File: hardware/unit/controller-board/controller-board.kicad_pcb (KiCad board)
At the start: 4 copper layers, 152 x 122.5 mm, 92 parts, among them J1 RJ45 LINK, J2 to RF board J14, Q4 BSS138BK, U1 VO2611, U11 LP2985-33, U12 TPS3823A-33, U13 74LVC1G74, U14 74LVC1G27, U15 74LVC1G02, U16 74LVC1G08, U2 VO2611, U3 VO2611, U4 PC817X, U5 74LVC1G14, U6 TLP176AM

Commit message: Pre-order review; RF board seat keep-outs; part reuse P-1 to P-5
- docs/reviews/2026-10-31-pre-order-review.md: review of all three boards
  before ordering (verify scripts, ERC/DRC, pin maps, BOM, fab and case,
  firmware against spec, open items, part reuse).
- RF board (D-189, M-107): no other-net copper or vias under the case
  seats at S1 to S6 and the SO-239/SMA GND bosses; relay NC pads (pad 12)
  in netclass RF. Re-routed, DRC 0.
- Part reuse (D-190, M-108): one value text for 2k2, 100n 50V X7R and
  10n 50V X7R; shack PC817X order code as the controller; shack U4/U9 in
  VSSOP-8 (TI DCU, Nexperia DC) with fixed fan-out, re-routed.
  Netlists rf15, ctl15, si17; ERC 0.

Co-Authored-By: Claude Opus 5.5 <noreply@anthropic.com>
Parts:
- C12: value 10n -> 10n 50V X7R

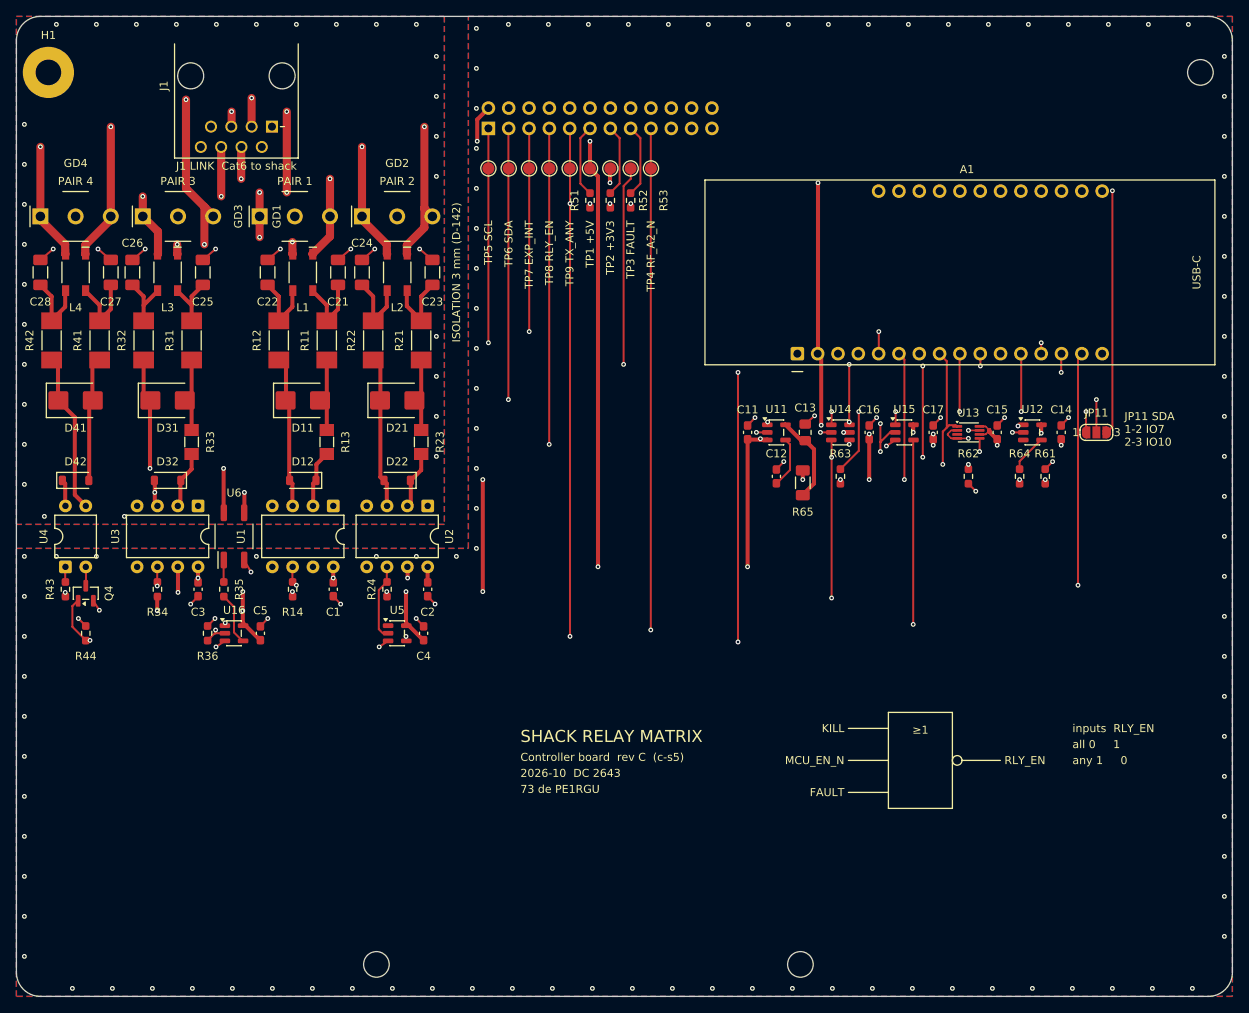
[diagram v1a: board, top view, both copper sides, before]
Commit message: S-1: FAULT to GPIO6, box fault 11, host clearfault
Hardware (D-191, M-109):
- Controller board: R66 1k from FAULT (U13 Q) to DevKit pin 11 (GPIO6).
  Schematic c15-fault-io6, netlist ctl16, layout c-s6, re-routed.
  ERC 0, DRC 0 violations and 0 unconnected. BOM: R66 on the 1k line.
- gen_controller_pcb.py splits a track where a same-net track ends on it.
- verify_logic.py checks R66 and FAULT_IO6.

Firmware:
- Box reads FAULT. After the self-test, FAULT = 1 gives fault 11
  (supervisor trip); READY stays open.
- New link command ClearFault (0x03): one LATCH_CLR edge, Ok if FAULT
  clears, else NotReady. No edge without a trip.
- Host clearfault also sends ClearFault when the box reports fault 11.
- Sim model, box target (GPIO6), 3 new tests.

Co-Authored-By: Claude Opus 5.5 <noreply@anthropic.com>
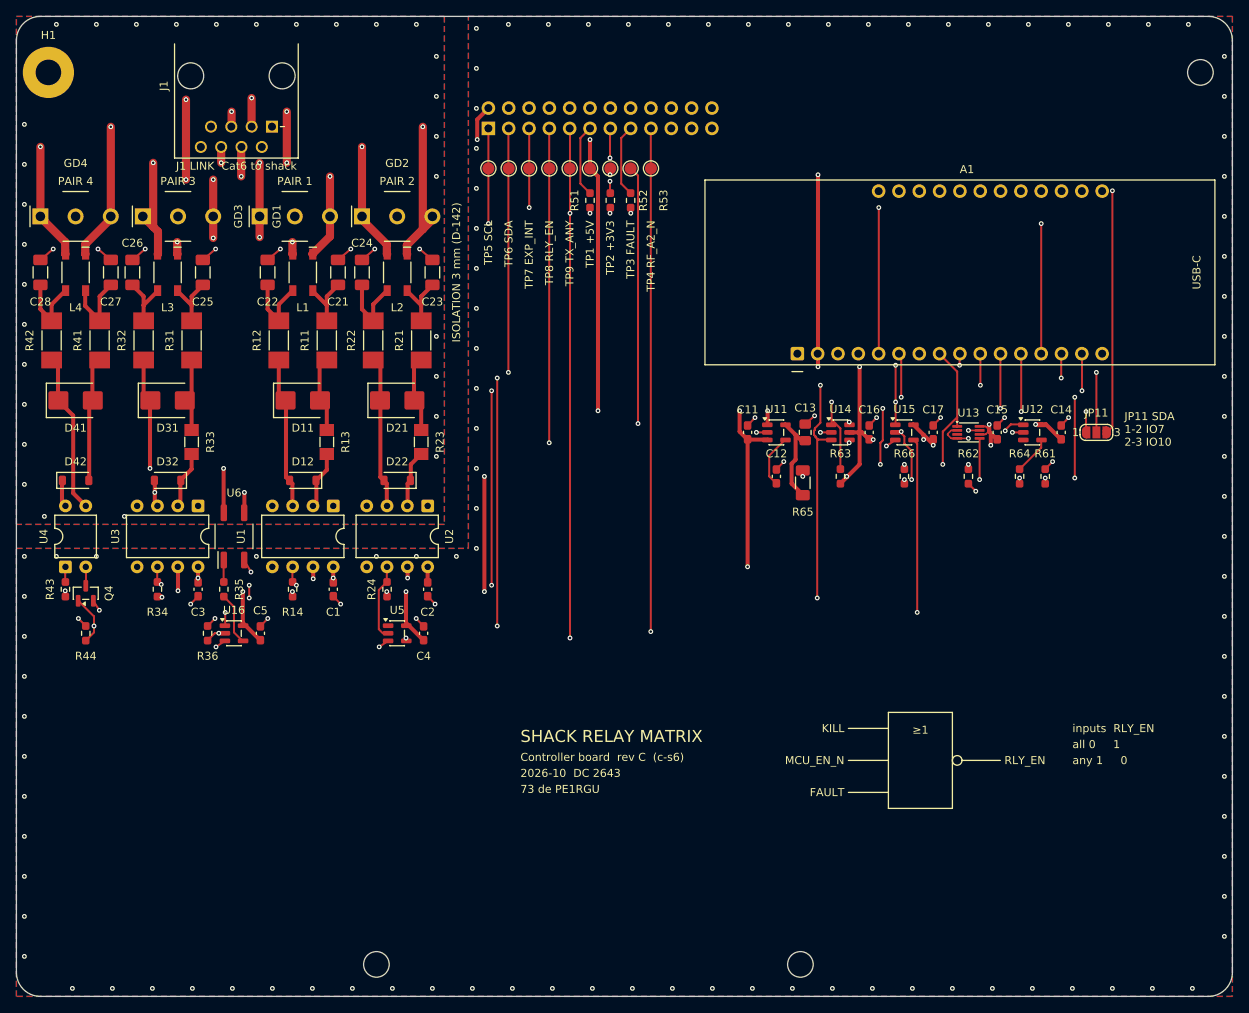
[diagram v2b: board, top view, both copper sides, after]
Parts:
- added R66: 1k, Resistor_SMD:R_0603_1608Metric_Pad0.98x0.95mm_HandSolder, F.Cu at (132.0, 75.5)
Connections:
- A1 pad 11: unconnected-(A1-IO6-Pad11) -> /MCU and safety gate/FAULT_IO6
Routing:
- net /MCU and safety gate/FAULT_IO6: track 0.00 -> 32.3 mm, vias 0 -> 4
- net /MCU and safety gate/WDI: track 34.7 -> 45.7 mm, vias 3 -> 5
- net /MCU and safety gate/FAULT: track 84.7 -> 88.7 mm
- net +5V: track 195.7 -> 199.2 mm, vias 11 -> 12
- net /MCU and safety gate/DATA_TX: track 164.2 -> 161.3 mm
- net +3V3: track 231.3 -> 229.1 mm, vias 22 -> 19
- net Net-(C23-Pad2): track 9.62 -> 7.67 mm
- net Net-(C21-Pad2): track 9.62 -> 7.67 mm
- net /Link and PTT/L3P: track 37.3 -> 38.9 mm, vias 4 -> 6
- net /MCU and safety gate/LATCH_CLR: track 19.8 -> 20.6 mm
- net /Link and PTT/RF_A2_N: track 120.3 -> 119.7 mm
- net /Link and PTT/TX_ANY: track 93.9 -> 94.5 mm
- net /Link and PTT/DATA_RX: track 129.5 -> 129.8 mm, vias 2 -> 4
- net /Link and PTT/R2_K0_DRV: track 9.18 -> 9.07 mm, vias 0 -> 2
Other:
- board text added: "Controller board rev C (c-s6)"
- board text removed: "Controller board rev C (c-s5)"

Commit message: S-2: SDA jumpers bridged 1-2 for RUST-1 by default
JP11 (controller) and JP61 (shack) use the Bridged12 solder jumper.
Pad 1 = SDA_IO10 (RUST-1), pad 3 = SDA_IO7 (RUST-2). Boards ship ready
for RUST-1; for RUST-2 cut 1-2 and bridge 2-3. New netlists ctl17 and
si18, new JP11/JP61 checks, boards re-routed, DRC clean. D-192, M-110.

Co-Authored-By: Claude Opus 5.5 <noreply@anthropic.com>
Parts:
- JP11: footprint Jumper:SolderJumper-3_P1.3mm_Open_RoundedPad1.0x1.5mm_NumberLabels -> Jumper:SolderJumper-3_P1.3mm_Bridged12_RoundedPad1.0x1.5mm_NumberLabels
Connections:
- JP11 pad 1: /MCU and safety gate/SDA_IO7 -> /MCU and safety gate/SDA_IO10
- JP11 pad 3: /MCU and safety gate/SDA_IO10 -> /MCU and safety gate/SDA_IO7
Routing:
- net /MCU and safety gate/WDI: track 45.7 -> 33.3 mm, vias 5 -> 3
- net /Link and PTT/KILL: track 139.2 -> 145.7 mm
- net /MCU and safety gate/FAULT_IO6: track 32.3 -> 26.5 mm, vias 4 -> 2
- net /MCU and safety gate/DATA_TX: track 161.3 -> 167.1 mm
- net /MCU and safety gate/FAULT: track 88.7 -> 94.0 mm
- net /MCU and safety gate/SDA_IO10: track 31.8 -> 34.8 mm, vias 1 -> 3
- net /MCU and safety gate/SDA_IO7: track 18.0 -> 20.6 mm
- net +5V: track 199.2 -> 196.6 mm
- net /Link and PTT/TX_ANY: track 94.5 -> 96.7 mm
- net Net-(C24-Pad1): track 9.58 -> 7.53 mm
- net Net-(C22-Pad1): track 9.58 -> 7.53 mm
- net Net-(C25-Pad2): track 7.67 -> 9.62 mm
- net +3V3: track 229.1 -> 231.0 mm, vias 19 -> 22
- net /Link and PTT/RF_A2_N: track 119.7 -> 121.5 mm
- net /MCU and safety gate/RLY_EN: track 77.3 -> 78.7 mm
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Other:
- board text added: "1-2 IO10"
- board text added: "2-3 IO7"
- board text added: "Controller board rev C (c-s7)"
- board text removed: "1-2 IO7"
- board text removed: "2-3 IO10"
- board text removed: "Controller board rev C (c-s6)"
